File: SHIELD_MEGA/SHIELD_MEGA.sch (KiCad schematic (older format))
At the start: 10 parts, among them J1 Conn_02x03_Odd_Even, J2 Conn_02x03_Odd_Even, J5 Conn_01x02_Male, SW1 SW_MEC_5E

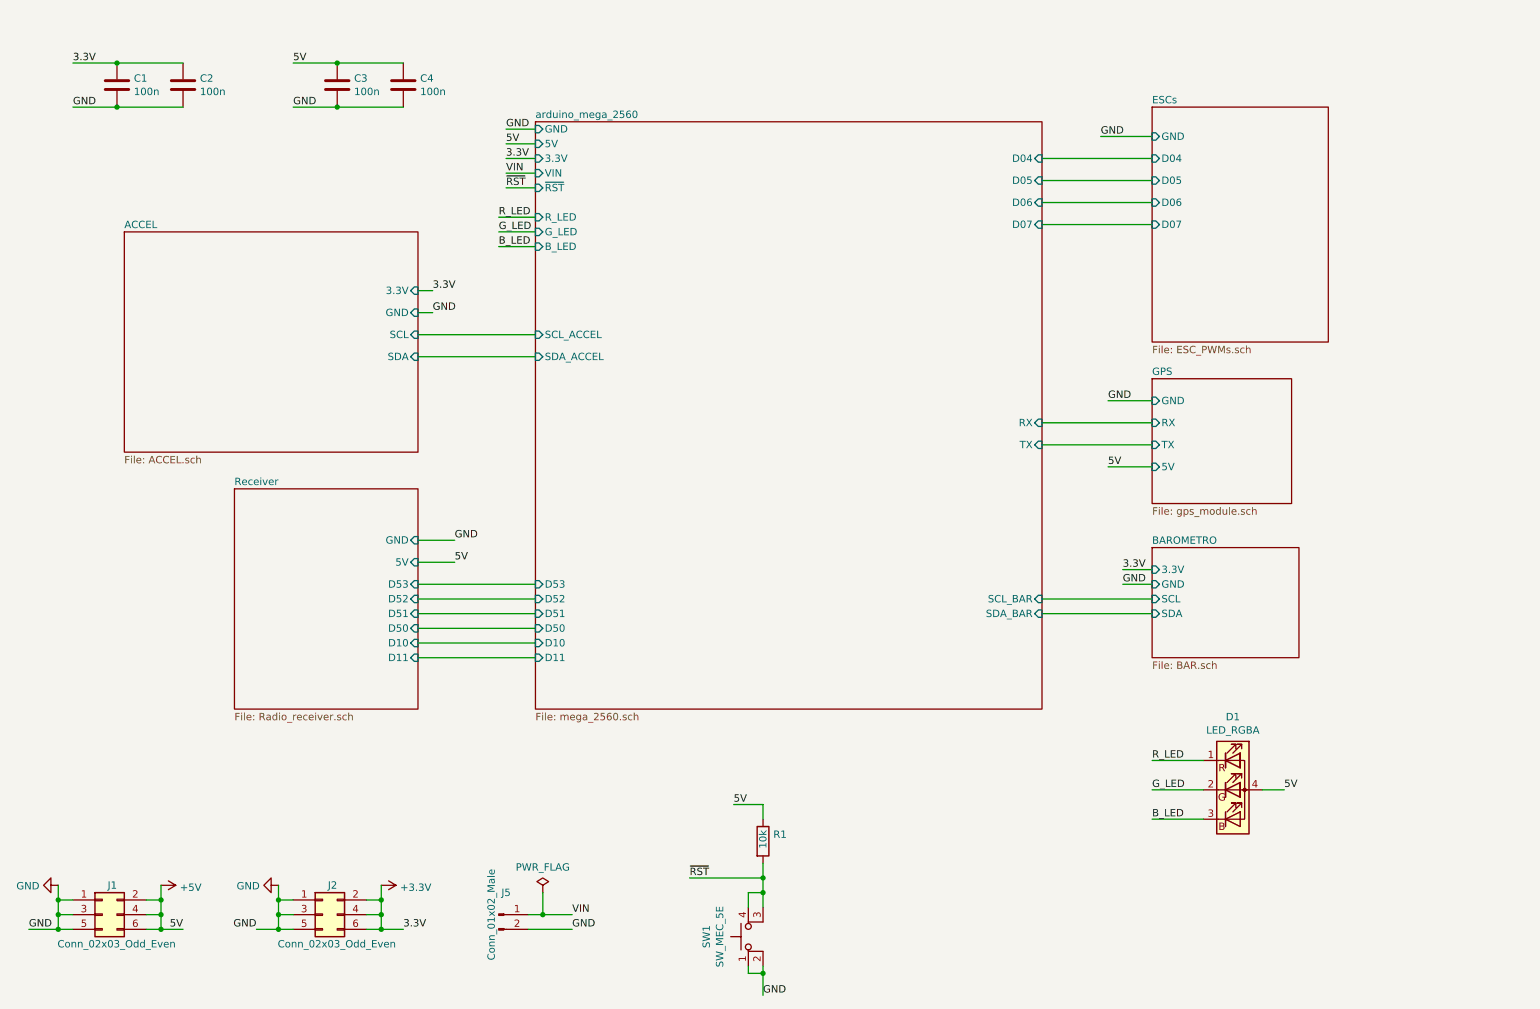
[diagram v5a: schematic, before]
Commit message: Inserting RGB led to notifications
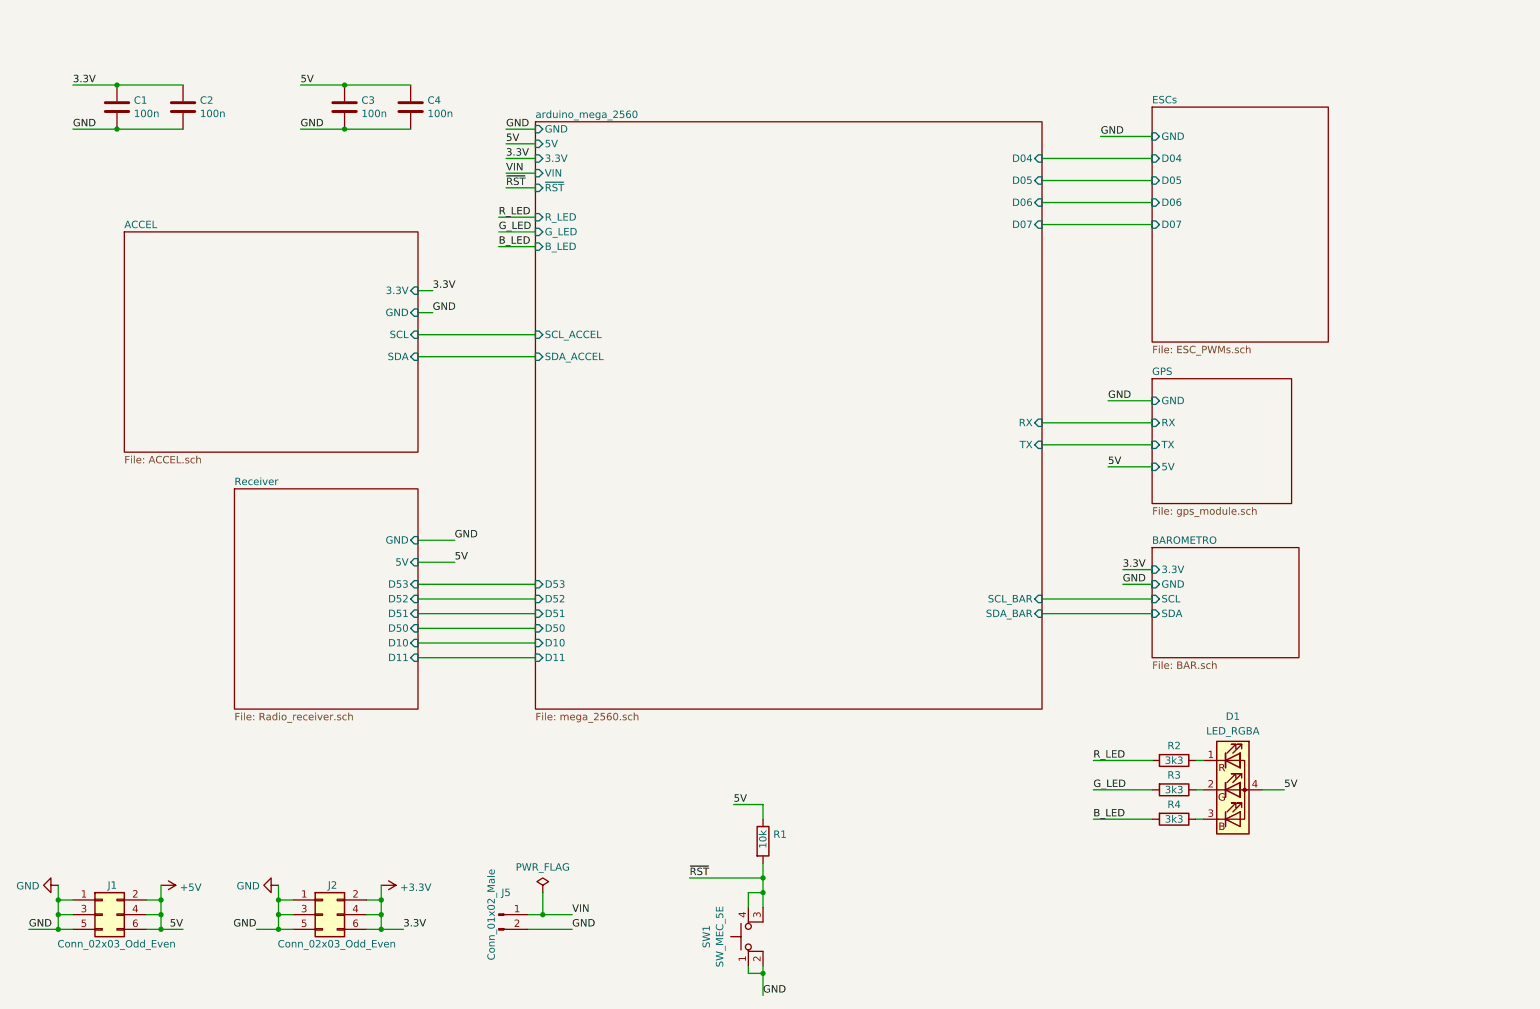
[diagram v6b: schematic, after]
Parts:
- added R2, R3, R4: 3k3, symbol Device:R
- D1: footprint (none) -> LED_SMD:LED_RGB_1210
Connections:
- net B_LED: now also R4.2; no longer D1.3 (BK)
- net G_LED: now also R3.2; no longer D1.2 (GK)
- net R_LED: now also R2.2; no longer D1.1 (RK)
- new net: D1.1 (RK), R2.1
- new net: D1.2 (GK), R3.1
- new net: D1.3 (BK), R4.1
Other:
- moved on the sheet: C1, C2, C3, C4
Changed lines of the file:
@@
 L Device:C C3
 U 1 1 619ADA37
-P 2900 1200
-F 0 "C3" H 3015 1246 50  0000 L CNN
-F 1 "100n" H 3015 1155 50  0000 L CNN
-F 2 "Capacitor_SMD:C_0805_2012Metric_Pad1.18x1.45mm_HandSolder" H 2938 1050 50  0001 C CNN
-F 3 "~" H 2900 1200 50  0001 C CNN
-	1    2900 1200
+P 2950 1350
+F 0 "C3" H 3065 1396 50  0000 L CNN
+F 1 "100n" H 3065 1305 50  0000 L CNN
+F 2 "Capacitor_SMD:C_0805_2012Metric_Pad1.18x1.45mm_HandSolder" H 2988 1200 50  0001 C CNN
+F 3 "~" H 2950 1350 50  0001 C CNN
+	1    2950 1350
 	1    0    0    -1
 $EndComp
@@
 L Device:C C4
 U 1 1 619AEAF2
-P 3350 1200
-F 0 "C4" H 3465 1246 50  0000 L CNN
-F 1 "100n" H 3465 1155 50  0000 L CNN
-F 2 "Capacitor_SMD:C_0805_2012Metric_Pad1.18x1.45mm_HandSolder" H 3388 1050 50  0001 C CNN
-F 3 "~" H 3350 1200 50  0001 C CNN
-	1    3350 1200
-	1    0    0    -1
-$EndComp
-Text Label 2600 1050 0    50   ~ 0
+P 3400 1350
+F 0 "C4" H 3515 1396 50  0000 L CNN
+F 1 "100n" H 3515 1305 50  0000 L CNN
+F 2 "Capacitor_SMD:C_0805_2012Metric_Pad1.18x1.45mm_HandSolder" H 3438 1200 50  0001 C CNN
+F 3 "~" H 3400 1350 50  0001 C CNN
+	1    3400 1350
+	1    0    0    -1
+$EndComp
+Text Label 2650 1200 0    50   ~ 0
 5V
 Wire Wire Line
-	2600 1050 2900 1050
-Wire Wire Line
-	2900 1050 3350 1050
-Connection ~ 2900 1050
-Text Label 2600 1350 0    50   ~ 0
-GND
-Wire Wire Line
-	2600 1350 2900 1350
-Wire Wire Line
-	2900 1350 3350 1350
-Connection ~ 2900 1350
+	2650 1200 2950 1200
+Wire Wire Line
+	2950 1200 3400 1200
+Connection ~ 2950 1200
+Text Label 2650 1500 0    50   ~ 0
+GND
+Wire Wire Line
+	2650 1500 2950 1500
+Wire Wire Line
+	2950 1500 3400 1500
+Connection ~ 2950 1500
 $Comp
 L Device:C C1
 U 1 1 619B7A55
-P 1400 1200
-F 0 "C1" H 1515 1246 50  0000 L CNN
-F 1 "100n" H 1515 1155 50  0000 L CNN
-F 2 "Capacitor_SMD:C_0805_2012Metric_Pad1.18x1.45mm_HandSolder" H 1438 1050 50  0001 C CNN
-F 3 "~" H 1400 1200 50  0001 C CNN
-	1    1400 1200
+P 1400 1350
+F 0 "C1" H 1515 1396 50  0000 L CNN
+F 1 "100n" H 1515 1305 50  0000 L CNN
+F 2 "Capacitor_SMD:C_0805_2012Metric_Pad1.18x1.45mm_HandSolder" H 1438 1200 50  0001 C CNN
+F 3 "~" H 1400 1350 50  0001 C CNN
+	1    1400 1350
 	1    0    0    -1
 $EndComp
@@
 L Device:C C2
 U 1 1 619B7A5B
-P 1850 1200
-F 0 "C2" H 1965 1246 50  0000 L CNN
-F 1 "100n" H 1965 1155 50  0000 L CNN
-F 2 "Capacitor_SMD:C_0805_2012Metric_Pad1.18x1.45mm_HandSolder" H 1888 1050 50  0001 C CNN
-F 3 "~" H 1850 1200 50  0001 C CNN
-	1    1850 1200
-	1    0    0    -1
-$EndComp
-Text Label 1100 1350 0    50   ~ 0
-GND
-Wire Wire Line
-	1100 1350 1400 1350
-Wire Wire Line
-	1400 1350 1850 1350
-Connection ~ 1400 1350
-Text Label 1100 1050 0    50   ~ 0
+P 1850 1350
+F 0 "C2" H 1965 1396 50  0000 L CNN
+F 1 "100n" H 1965 1305 50  0000 L CNN
+F 2 "Capacitor_SMD:C_0805_2012Metric_Pad1.18x1.45mm_HandSolder" H 1888 1200 50  0001 C CNN
+F 3 "~" H 1850 1350 50  0001 C CNN
+	1    1850 1350
+	1    0    0    -1
+$EndComp
+Text Label 1100 1500 0    50   ~ 0
+GND
+Wire Wire Line
+	1100 1500 1400 1500
+Wire Wire Line
+	1400 1500 1850 1500
+Connection ~ 1400 1500
+Text Label 1100 1200 0    50   ~ 0
 3.3V
 Wire Wire Line
-	1100 1050 1400 1050
-Wire Wire Line
-	1400 1050 1850 1050
-Connection ~ 1400 1050
+	1100 1200 1400 1200
+Wire Wire Line
+	1400 1200 1850 1200
+Connection ~ 1400 1200
 $Comp
 L power:GND #PWR02
@@
 U 1 1 619C80CD
 P 9000 6000
-F 0 "D1" H 9000 6497 50  0000 C CNN
-F 1 "LED_RGBA" H 9000 6406 50  0000 C CNN
-F 2 "" H 9000 5950 50  0001 C CNN
+F 0 "D1" H 9000 6500 50  0000 C CNN
+F 1 "LED_RGBA" H 9000 6400 50  0000 C CNN
+F 2 "LED_SMD:LED_RGB_1210" H 9000 5950 50  0001 C CNN
 F 3 "~" H 9000 5950 50  0001 C CNN
 	1    9000 6000
@@
 Wire Wire Line
 	9350 6000 9200 6000
-Text Label 8450 5800 0    50   ~ 0
+Text Label 8050 5800 0    50   ~ 0
 R_LED
-Wire Wire Line
-	8450 5800 8800 5800
-Wire Wire Line
-	8450 6000 8800 6000
-Text Label 8450 6000 0    50   ~ 0
+Text Label 8050 6000 0    50   ~ 0
 G_LED
-Text Label 8450 6200 0    50   ~ 0
+Text Label 8050 6200 0    50   ~ 0
 B_LED
-Wire Wire Line
-	8450 6200 8800 6200
 Text Label 4000 2100 0    50   ~ 0
 R_LED
@@
 Wire Wire Line
 	4000 2300 4250 2300
+$Comp
+L Device:R R2
+U 1 1 619DB27E
+P 8600 5800
+F 0 "R2" V 8500 5800 50  0000 C CNN
+F 1 "3k3" V 8600 5800 50  0000 C CNN
+F 2 "" V 8530 5800 50  0001 C CNN
+F 3 "~" H 8600 5800 50  0001 C CNN
+	1    8600 5800
+	0    1    1    0
+$EndComp
+$Comp
+L Device:R R3
+U 1 1 619DBAEB
+P 8600 6000
+F 0 "R3" V 8500 6000 50  0000 C CNN
+F 1 "3k3" V 8600 6000 50  0000 C CNN
+F 2 "" V 8530 6000 50  0001 C CNN
+F 3 "~" H 8600 6000 50  0001 C CNN
+	1    8600 6000
+	0    1    1    0
+$EndComp
+$Comp
+L Device:R R4
+U 1 1 619DEF92
+P 8600 6200
+F 0 "R4" V 8500 6200 50  0000 C CNN
+F 1 "3k3" V 8600 6200 50  0000 C CNN
+F 2 "" V 8530 6200 50  0001 C CNN
+F 3 "~" H 8600 6200 50  0001 C CNN
+	1    8600 6200
+	0    1    1    0
+$EndComp
+Wire Wire Line
+	8750 5800 8800 5800
+Wire Wire Line
+	8750 6000 8800 6000
+Wire Wire Line
+	8750 6200 8800 6200
+Wire Wire Line
+	8050 6200 8450 6200
+Wire Wire Line
+	8050 6000 8450 6000
+Wire Wire Line
+	8050 5800 8450 5800
 $EndSCHEMATC

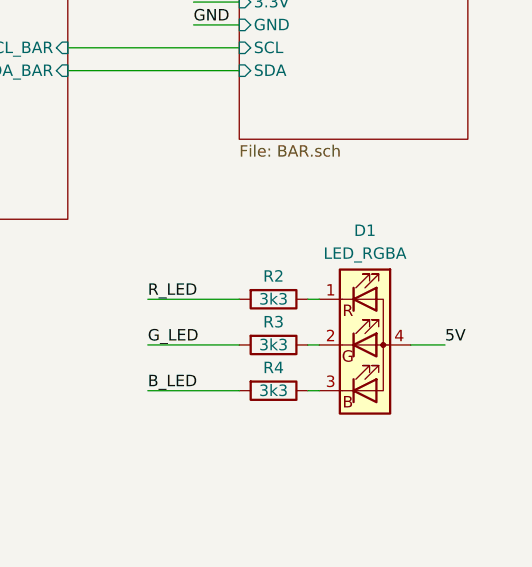
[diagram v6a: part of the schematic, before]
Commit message: Adding footprint to RGB led resistors
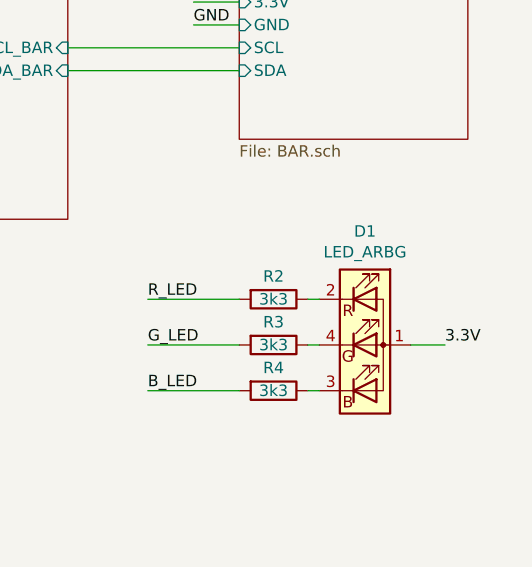
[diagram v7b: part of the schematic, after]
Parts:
- removed D1: LED_RGBA, LED_SMD:LED_RGB_1210, symbol Device:LED_RGBA
- added D1: LED_ARBG, LED_ARBG:LED_LL-R3528RGBC-008-B, symbol Device:LED_ARBG
- R2, R3, R4: footprint (none) -> Resistor_SMD:R_0805_2012Metric_Pad1.20x1.40mm_HandSolder
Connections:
- net +3V3: now also D1.1 (A)
- net at R2.1: now also D1.2 (RK)
- net at R3.1: now also D1.4 (GK)
- net at R4.1: now also D1.3 (BK)
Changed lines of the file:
@@
 	1000 6650 1000 6750
 Connection ~ 1000 6750
-$Comp
-L Device:LED_RGBA D1
-U 1 1 619C80CD
-P 9000 6000
-F 0 "D1" H 9000 6500 50  0000 C CNN
-F 1 "LED_RGBA" H 9000 6400 50  0000 C CNN
-F 2 "LED_SMD:LED_RGB_1210" H 9000 5950 50  0001 C CNN
-F 3 "~" H 9000 5950 50  0001 C CNN
-	1    9000 6000
-	1    0    0    -1
-$EndComp
-Text Label 9350 6000 0    50   ~ 0
-5V
 Wire Wire Line
 	9350 6000 9200 6000
@@
 F 0 "R2" V 8500 5800 50  0000 C CNN
 F 1 "3k3" V 8600 5800 50  0000 C CNN
-F 2 "" V 8530 5800 50  0001 C CNN
+F 2 "Resistor_SMD:R_0805_2012Metric_Pad1.20x1.40mm_HandSolder" V 8530 5800 50  0001 C CNN
 F 3 "~" H 8600 5800 50  0001 C CNN
 	1    8600 5800
@@
 F 0 "R3" V 8500 6000 50  0000 C CNN
 F 1 "3k3" V 8600 6000 50  0000 C CNN
-F 2 "" V 8530 6000 50  0001 C CNN
+F 2 "Resistor_SMD:R_0805_2012Metric_Pad1.20x1.40mm_HandSolder" V 8530 6000 50  0001 C CNN
 F 3 "~" H 8600 6000 50  0001 C CNN
 	1    8600 6000
@@
 F 0 "R4" V 8500 6200 50  0000 C CNN
 F 1 "3k3" V 8600 6200 50  0000 C CNN
-F 2 "" V 8530 6200 50  0001 C CNN
+F 2 "Resistor_SMD:R_0805_2012Metric_Pad1.20x1.40mm_HandSolder" V 8530 6200 50  0001 C CNN
 F 3 "~" H 8600 6200 50  0001 C CNN
 	1    8600 6200
@@
 Wire Wire Line
 	8050 5800 8450 5800
+$Comp
+L Device:LED_ARBG D1
+U 1 1 61A02B56
+P 9000 6000
+F 0 "D1" H 9000 6497 50  0000 C CNN
+F 1 "LED_ARBG" H 9000 6406 50  0000 C CNN
+F 2 "LED_ARBG:LED_LL-R3528RGBC-008-B" H 9000 5950 50  0001 C CNN
+F 3 "~" H 9000 5950 50  0001 C CNN
+	1    9000 6000
+	1    0    0    -1
+$EndComp
+Text Label 9350 6000 0    50   ~ 0
+3.3V
 $EndSCHEMATC
